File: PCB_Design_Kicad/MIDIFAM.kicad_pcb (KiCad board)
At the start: 2 copper layers, 81 parts, among them J1 PWR_IN, J11 Conn_01x07, J12 Conn_01x07, J13 Conn_01x07, J14 Conn_01x07, J15 Conn_01x07, J16 Conn_01x07, J17 MIDI in, J2 ISP connector, J3 Voct_A, J4 Trig_A, J5 Vel_A, J6 Voct_B, J7 Trig_B, J8 Vel_B, J9 Adv/Clock, SW1 midi learn, SW2 re-sync, SW3 seq. mode, U1 TL072, U2 MCP4822, U3 ATmega328, U4 78L05, U5 6N137

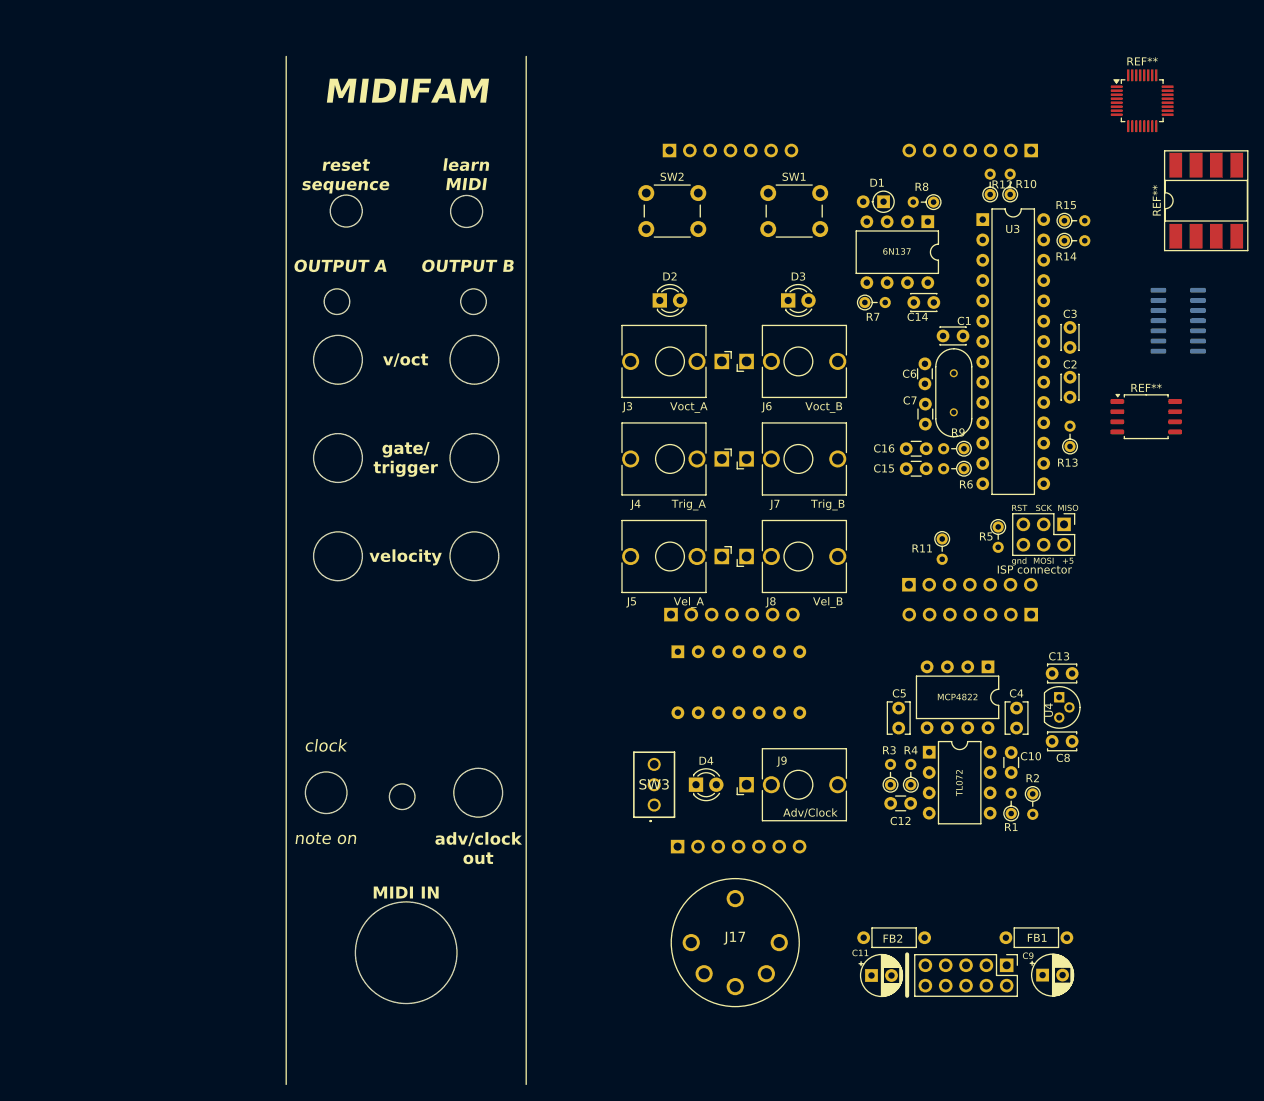
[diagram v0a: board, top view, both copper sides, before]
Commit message: SMD pcb, routable and with vias
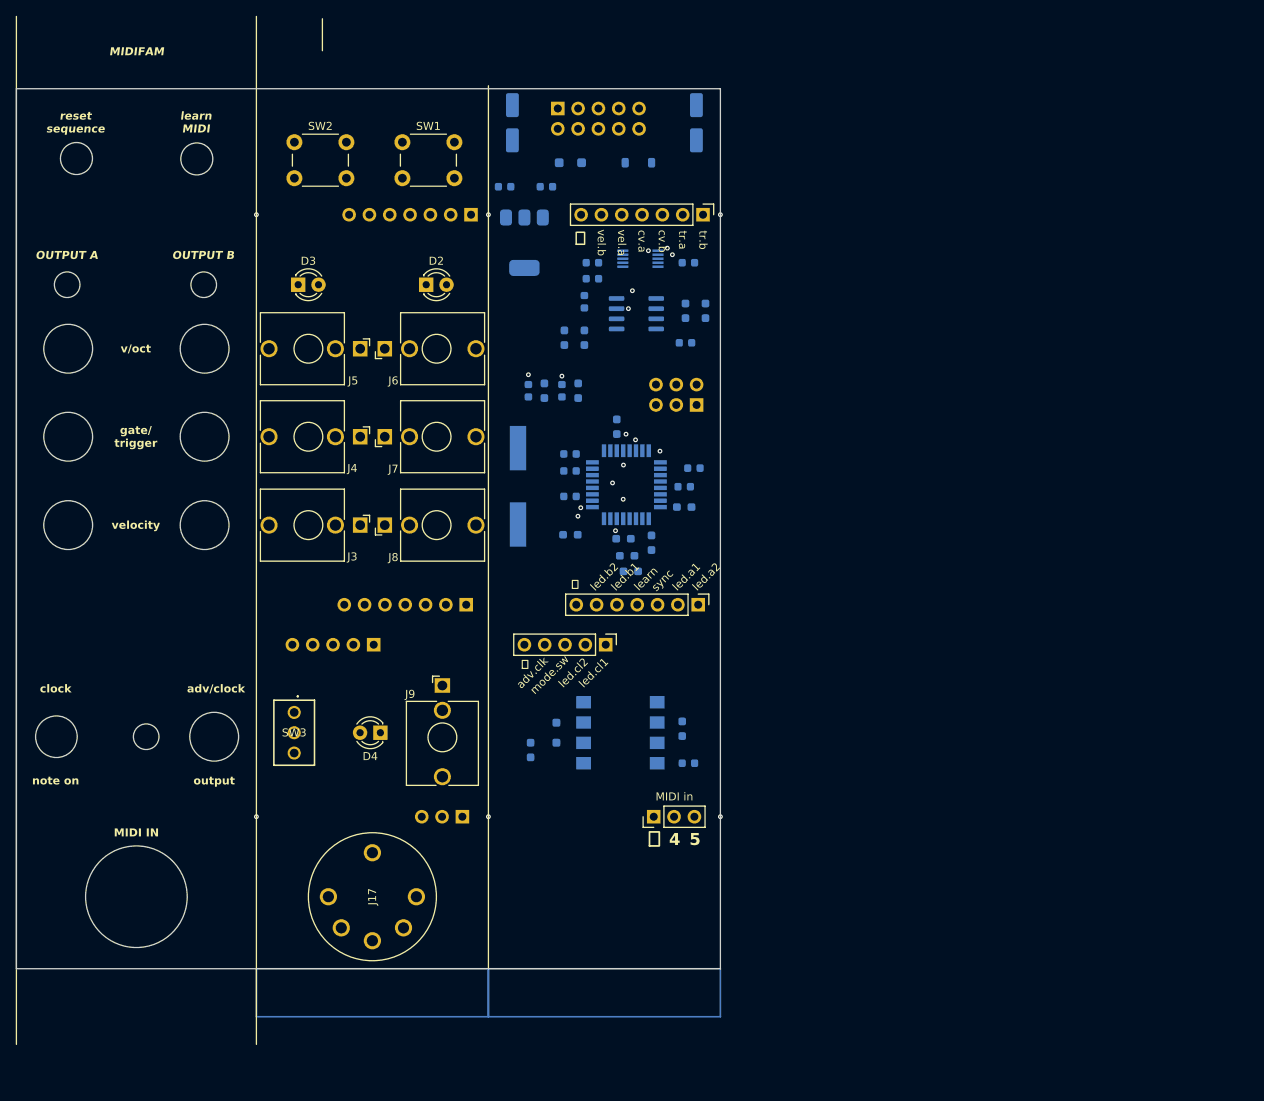
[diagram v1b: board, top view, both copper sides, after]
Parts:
- removed FB1, FB2: FerriteBead_Small, Inductor_THT:L_Axial_L5.3mm_D2.2mm_P7.62mm_Horizontal_Vishay_IM-1
- removed J11, J12, J13: Conn_01x07, Connector_PinHeader_2.54mm:PinHeader_1x07_P2.54mm_Vertical
- removed the REF** at (165.5, 26.5)
- removed the REF** at (173.5, 39.0)
- removed the REF** at (166.0, 66.0)
- removed the REF** at (170.0, 54.0)
- removed the REF** at (107.5, 95.4)
- removed U3: ATmega328, Package_DIP:DIP-28_W7.62mm
- removed U4: 78L05, Package_TO_SOT_THT:TO-92
- added C17: 1u, Capacitor_SMD:C_0603_1608Metric, B.Cu at (108.8, 46.8)
- added D5: rpp diode, Diode_SMD:D_SOD-123F, B.Cu at (94.0, 34.2)
- added D6: rpp diode, Diode_SMD:D_SOD-123, B.Cu at (102.5, 34.2)
- added IC1: DAC8562SDGSR, SamacSys_Parts:SOP50P490X110-10N, B.Cu at (102.8, 46.2)
- added J10: midi, Connector_PinHeader_2.54mm:PinHeader_1x03_P2.54mm_Vertical, F.Cu at (104.4, 116.0)
- added J18: Conn_01x05, Connector_PinHeader_2.54mm:PinHeader_1x05_P2.54mm_Vertical, F.Cu at (98.4, 94.5)
- added J19: Conn_01x07, Connector_PinHeader_2.54mm:PinHeader_1x07_P2.54mm_Vertical, B.Cu at (81.6, 40.8)
- added J20: Conn_01x05, Connector_PinHeader_2.54mm:PinHeader_1x05_P2.54mm_Vertical, B.Cu at (69.4, 94.5)
- added J21: midi, Connector_PinHeader_2.54mm:PinHeader_1x03_P2.54mm_Vertical, B.Cu at (80.5, 116.0)
- added U6: ATmega328-A, Package_QFP:TQFP-32_7x7mm_P0.8mm, B.Cu at (101.0, 74.5)
- C1, C14, C2, C3: footprint Capacitor_THT:C_Disc_D3.0mm_W2.0mm_P2.50mm -> Capacitor_SMD:C_0603_1608Metric; moved to B.Cu
- C10, C12, C6, C7: footprint Capacitor_THT:C_Disc_D3.0mm_W1.6mm_P2.50mm -> Capacitor_SMD:C_0603_1608Metric; moved to B.Cu
- C11, C9: footprint Capacitor_THT:CP_Radial_D5.0mm_P2.50mm -> Capacitor_SMD:CP_Elec_5x5.3; moved to B.Cu
- C13: value 0.1u -> 1u; footprint Capacitor_THT:C_Disc_D3.4mm_W2.1mm_P2.50mm -> Capacitor_SMD:C_0603_1608Metric; moved to B.Cu
- C15, C16: value 18p -> ??; footprint Capacitor_THT:C_Disc_D3.0mm_W1.6mm_P2.50mm -> Capacitor_SMD:C_0603_1608Metric; moved to B.Cu
- C4, C5: footprint Capacitor_THT:C_Disc_D3.8mm_W2.6mm_P2.50mm -> Capacitor_SMD:C_0603_1608Metric; moved to B.Cu
- C8: value 0.33U -> 1u; footprint Capacitor_THT:C_Disc_D3.4mm_W2.1mm_P2.50mm -> Capacitor_SMD:C_0603_1608Metric; moved to B.Cu
- D1: footprint Diode_THT:D_DO-35_SOD27_P2.54mm_Vertical_AnodeUp -> Diode_SMD:D_SOD-323_HandSoldering; moved to B.Cu
- J1, J2: moved to B.Cu
- J14, J15: moved to F.Cu
- J9: value Adv/Clock -> adv_clock_out
- R1, R10, R13, R15, R2, R3, R4, R6, R7, R8, R9: footprint Resistor_THT:R_Axial_DIN0204_L3.6mm_D1.6mm_P2.54mm_Vertical -> Resistor_SMD:R_0603_1608Metric_Pad0.98x0.95mm_HandSolder; moved to B.Cu
- R11, R12: value 220R -> 10k; footprint Resistor_THT:R_Axial_DIN0204_L3.6mm_D1.6mm_P2.54mm_Vertical -> Resistor_SMD:R_0603_1608Metric_Pad0.98x0.95mm_HandSolder; moved to B.Cu
- R14, R5: value 10k -> 220R; footprint Resistor_THT:R_Axial_DIN0204_L3.6mm_D1.6mm_P2.54mm_Vertical -> Resistor_SMD:R_0603_1608Metric_Pad0.98x0.95mm_HandSolder; moved to B.Cu
- U1: footprint Package_DIP:DIP-8_W7.62mm -> Package_SO:SOIC-8_3.9x4.9mm_P1.27mm; moved to B.Cu
- U2: value MCP4822 -> MCP1703Ax-500xxDB; footprint Package_DIP:DIP-8_W7.62mm -> Package_TO_SOT_SMD:SOT-223-3_TabPin2; moved to B.Cu
- U5: footprint Package_DIP:DIP-8_W7.62mm -> SamacSys_Parts:SOP254P1005X465-8N; moved to B.Cu
- xtal1: footprint CrystalRes:XTAL_HC49P488W46L1150T500H350 -> SamacSys_Parts:XT9M20ANA20M; moved to B.Cu
- moved C9 125.5 mm to (86.8, 29.2), turned to 90 degrees
- moved J1 120.9 mm to (92.5, 27.5)
- moved C11 108.8 mm to (109.8, 29.2), turned to -90 degrees
- moved C8 97.4 mm to (85.8, 37.2)
- moved C13 89.6 mm to (91.0, 37.2), turned to 0 degrees
- moved R8 85.0 mm to (89.0, 107.7), turned to 90 degrees
- moved R2 81.7 mm to (93.3, 56.1)
- moved R1 79.9 mm to (95.8, 56.1)
- moved C10 79.4 mm to (95.8, 51.6), turned to -90 degrees
- moved U2 78.5 mm to (88.3, 44.2)
- moved D1 78.0 mm to (92.3, 105.5), turned to 90 degrees
- moved C4 77.2 mm to (96.8, 48.8), turned to 180 degrees
- moved U5 74.5 mm to (100.3, 105.5), turned to 0 degrees
- moved R14 71.9 mm to (94.0, 80.8), turned to 180 degrees
- moved J14 70.4 mm to (110.0, 89.5), turned to -90 degrees
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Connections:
- C4 pad 1: /dac_a -> /DAC_OUT_A
- C5 pad 1: /dac_b -> /DAC_OUT_B
- J14 pad 1: /learn_sw_b -> /led_a2_b
- J14 pad 2: /sync_sw_b -> /led_a1_b
- J14 pad 3: /led_a1_b -> /sync_sw_b
- J14 pad 4: /led_a2_b -> /learn_sw_b
- J15 pad 1: /voct_a_b -> /trig_b_b
- J15 pad 2: /voct_b_b -> /trig_a_b
- J15 pad 3: /trig_a_b -> /voct_b_b
- J15 pad 4: /trig_b_b -> /voct_a_b
- J16 pad 1: /led_cl1_b -> /IO Control PCB/led_a2_f
- J16 pad 2: /led_cl2_b -> /IO Control PCB/led_a1_f
- J16 pad 3: /adv_clock_b -> /IO Control PCB/sync_sw_f
- J16 pad 4: /seq_mode_sw_b -> /IO Control PCB/learn_sw_f
- J16 pad 5: /midi4 -> /IO Control PCB/led_b1_f
- J16 pad 6: /midi5 -> /IO Control PCB/led_b2_f
- J17 pad 2: unconnected-(J17-Pad2) -> /IO Control PCB/midi5_f
- J17 pad 5: /IO Control PCB/midi5_f -> unconnected-(J17-Pad5)
- R11 pad 1: Net-(U3-PC1) -> 5V
- R11 pad 2: /led_cl2_b -> /sync_sw_b
- R12 pad 1: Net-(U3-PD2) -> 5V
- R12 pad 2: /led_b2_b -> /learn_sw_b
- R13 pad 1: /seq_mode_sw_b -> /RESET
- R14 pad 1: /sync_sw_b -> Net-(U6-PD2)
- R14 pad 2: 5V -> /led_b2_b
- R15 pad 1: /learn_sw_b -> /seq_mode_sw_b
- R5 pad 1: /RESET -> Net-(U6-PC1)
- R5 pad 2: 5V -> /led_cl2_b
- U1 pad 3: /dac_b -> /DAC_OUT_B
- U1 pad 5: /dac_a -> /DAC_OUT_A
- U2 pad 1: 5V -> +12V
- U2 pad 2: /CS -> GND
- U2 pad 3: /SCK -> 5V
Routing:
- net 5V: vias 0 -> 2
- net /voct_b_b: vias 0 -> 1
- net /voct_a_b: vias 0 -> 1
- net /vel_b_b: vias 0 -> 1
- net /vel_a_b: vias 0 -> 1
- net /trig_b_b: vias 0 -> 1
- net /trig_a_b: vias 0 -> 1
- net /seq_mode_sw_b: vias 0 -> 1
- net /adv_clock_b: vias 0 -> 1
- net /SCK: vias 0 -> 2
- net /RESET: vias 0 -> 1
- net /MOSI: vias 0 -> 1
- net /CS: vias 0 -> 2
- net (no net): vias 0 -> 6
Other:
- board outline added: 88 x 110 mm
- board text added: "-12V"
- board text added: "4"
- board text added: "5"
- board text added: "ISP conn."
- board text added: "MIDI in"
- board text added: "Remove PCB-mount MIDI jack and hard wire"
- board text added: "adv.clk"
- board text added: "adv/clock"
- board text added: "cv.a"
- board text added: "cv.b"
- board text added: "learn"
- board text added: "led.a1"
- board text added: "led.a2"
- board text added: "led.b1"
- board text added: "led.b2"
- board text added: "led.cl1"
- board text added: "led.cl2"
- board text added: "mode.sw"
- board text added: "output"
- board text added: "sync"
- board text added: "tr.a"
- board text added: "tr.b"
- board text added: "vel.a"
- board text added: "vel.b"
- board text added: "⏚"
- board text removed: "+5"
- board text removed: "MISO"
- board text removed: "MOSI"
- board text removed: "RST"
- board text removed: "SCK"
- board text removed: "adv/clock out"
- board text removed: "gnd"

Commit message: routed SMD
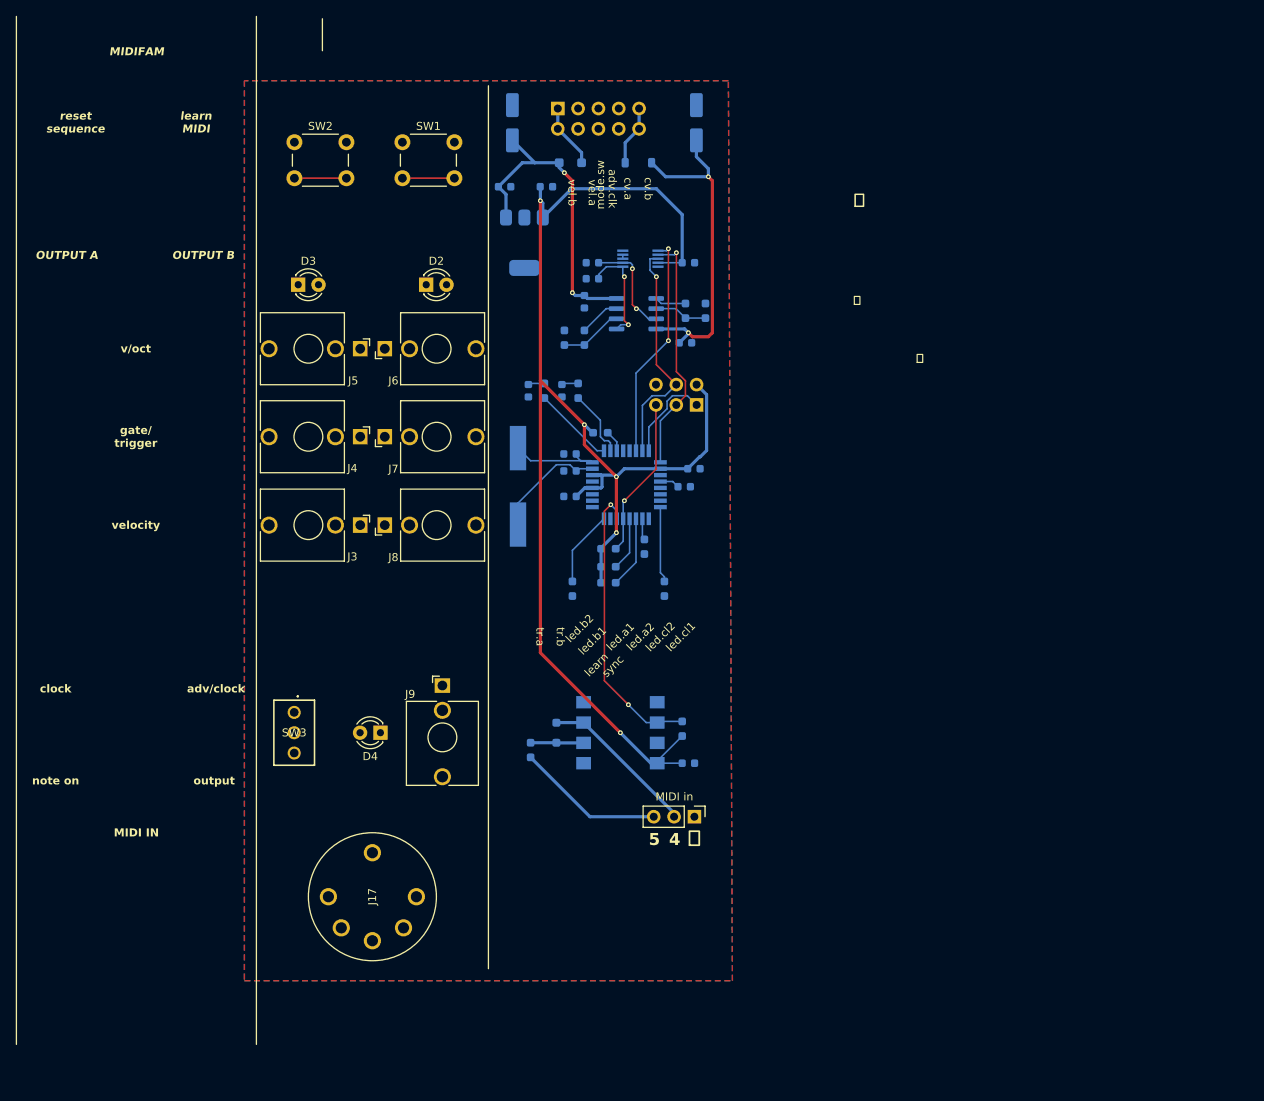
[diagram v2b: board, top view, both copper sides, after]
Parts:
- removed J14, J15, J16, J19: Conn_01x07, Connector_PinHeader_2.54mm:PinHeader_1x07_P2.54mm_Vertical
- removed J18, J20: Conn_01x05, Connector_PinHeader_2.54mm:PinHeader_1x05_P2.54mm_Vertical
- removed J21: midi, Connector_PinHeader_2.54mm:PinHeader_1x03_P2.54mm_Vertical
- removed REF** (x7): Mounting_Hole_Jack, WeirdVibes_Eurorack:Mounting_Hole_Jack
- removed REF** (x3): Panel_Mounting_Hole_Circle, WeirdVibes_Eurorack:Panel_Mounting_Hole_Circle
- removed REF** (x3): MountingHole_6mm, MountingHole:MountingHole_6mm
- removed REF**: Mounting_Hole_Switch, WeirdVibes_Eurorack:Mounting_Hole_Switch
- moved R5 10.5 mm to (105.8, 87.5), turned to -90 degrees
- moved R14 6.75 mm to (94.3, 87.5), turned to -90 degrees
- moved J10 5.08 mm to (109.5, 116.0), turned to -90 degrees
- moved R11 3.14 mm to (98.8, 86.8)
- moved R12 2.71 mm to (98.8, 84.8)
- moved R13 2.26 mm to (98.8, 82.5)
- moved R15 2.18 mm to (97.8, 68.0), turned to 180 degrees
- moved R10 1.02 mm to (103.3, 82.2)
- moved C2 0.07 mm to (109.5, 72.5)
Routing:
- net 5V: track 0.00 -> 179.7 mm, vias 2 -> 5
- net -12V: track 0.00 -> 42.1 mm, vias 0 -> 2
- net +12V: track 0.00 -> 39.8 mm, vias 0 -> 2
- net /UART_Rx: track 0.00 -> 36.0 mm, vias 0 -> 2
- net /SCK: track 0.00 -> 30.4 mm, vias 2 -> 1
- net /MOSI: track 0.00 -> 29.0 mm
- net /CS: track 0.00 -> 28.3 mm
- net /RESET: track 0.00 -> 20.1 mm
- net /midi4: track 0.00 -> 19.4 mm
- net /midi5: track 0.00 -> 18.5 mm
- net Net-(U6-XTAL1/PB6): track 0.00 -> 14.0 mm
- net /DAC_OUT_A: track 0.00 -> 13.2 mm, vias 0 -> 2
- net /DAC_OUT_B: track 0.00 -> 13.0 mm, vias 0 -> 2
- net Net-(U6-XTAL2/PB7): track 0.00 -> 12.1 mm
- net /MISO: track 0.00 -> 11.6 mm
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- added copper zone on B.Cu, net GND
- added copper zone on F.Cu, net GND
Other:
- board outline removed
- board text added: "+"
- board text removed: "Remove PCB-mount MIDI jack and hard wire"

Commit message: better routing
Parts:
- removed J17: MIDI in, SamacSys_Parts:SD-50BV
- added J11: back bottom, Connector_PinHeader_2.54mm:PinHeader_1x11_P2.54mm_Vertical, F.Cu at (85.6, 93.5)
- added J12: front bottom, Connector_PinSocket_2.54mm:PinSocket_1x11_P2.54mm_Vertical, B.Cu at (56.6, 93.5)
- added J13: back top, Connector_PinHeader_2.54mm:PinHeader_1x07_P2.54mm_Vertical, F.Cu at (94.2, 41.0)
- added J14: front top, Connector_PinSocket_2.54mm:PinSocket_1x07_P2.54mm_Vertical, B.Cu at (65.2, 41.0)
- SW1: value midi learn -> re-sync
- SW2: value re-sync -> midi learn
- moved J10 9.13 mm to (102.8, 109.8)
- moved C14 4.23 mm to (108.8, 105.1)
- moved D1 4.23 mm to (92.3, 101.3)
- moved R7 4.23 mm to (108.0, 100.8)
- moved U5 4.23 mm to (100.3, 101.3)
- moved R8 4.23 mm to (89.0, 103.4)
- moved R14 2.92 mm to (91.8, 86.0)
- moved D4 2.00 mm to (70.3, 103.5)
- moved J9 2.00 mm to (78.0, 104.1)
- moved SW3 2.00 mm to (59.5, 101.0)
- moved R1 0.80 mm to (96.3, 55.5)
- moved R2 0.80 mm to (93.8, 55.5)
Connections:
- SW1 pad 2: /IO Control PCB/learn_sw_f -> /IO Control PCB/sync_sw_f
- SW2 pad 2: /IO Control PCB/sync_sw_f -> /IO Control PCB/learn_sw_f
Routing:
- net /adv_clock_b: track 0.00 -> 38.4 mm
- net /seq_mode_sw_b: track 2.72 -> 36.8 mm
- net 5V: track 179.7 -> 154.6 mm
- net /vel_a_b: track 1.89 -> 25.7 mm
- net /vel_b_b: track 1.86 -> 24.7 mm
- net /trig_b_b: track 0.00 -> 22.4 mm
- net /voct_a_b: track 5.15 -> 27.3 mm
- net /trig_a_b: track 0.00 -> 19.8 mm
- net /led_cl1_b: track 0.00 -> 18.9 mm
- net /led_b1_b: track 0.00 -> 17.2 mm
- net /led_a2_b: track 0.00 -> 15.1 mm
- net /voct_b_b: track 3.92 -> 15.9 mm
- net /led_a1_b: track 0.00 -> 11.3 mm
- net /learn_sw_b: track 6.72 -> 17.1 mm
- net /midi5: track 18.5 -> 11.0 mm
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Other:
- board outline added: 58 x 87.2 mm
- board text added: "1"
- board text added: "2"
- board text added: "3"
- board text added: "6"
- board text removed: "+"
- board text removed: "MIDI IN"
- board text removed: "MIDIFAM"
- board text removed: "OUTPUT A"
- board text removed: "OUTPUT B"
- board text removed: "adv/clock"
- board text removed: "clock"
- board text removed: "gate/ trigger"
- board text removed: "learn MIDI"
- board text removed: "note on"
- board text removed: "output"
- board text removed: "reset sequence"
- board text removed: "v/oct"
- board text removed: "velocity"
